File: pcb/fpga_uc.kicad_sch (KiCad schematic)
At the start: 1 part

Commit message: kicad said I needed to save
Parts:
- U?: value (none) -> XC7A100T-FTG256
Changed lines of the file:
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@@
       (effects (font (size 1.27 1.27)) (justify right))
     )
-    (property "Value" "" (id 1) (at 67.31 81.9149 0)
+    (property "Value" "XC7A100T-FTG256" (id 1) (at 67.31 81.9149 0)
       (effects (font (size 1.27 1.27)) (justify right))
     )

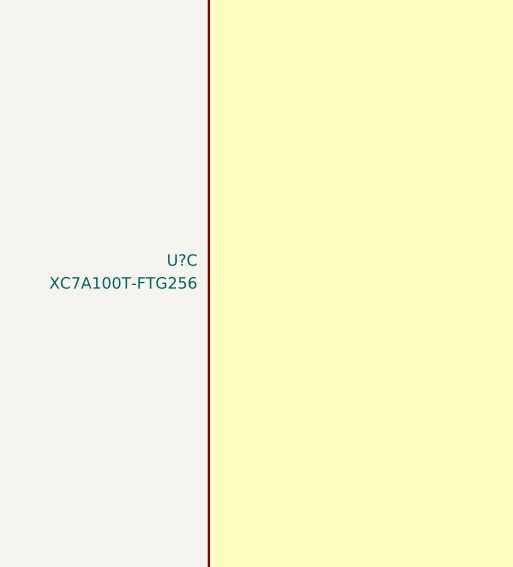
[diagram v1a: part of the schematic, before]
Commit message: add flash memory component for fpga
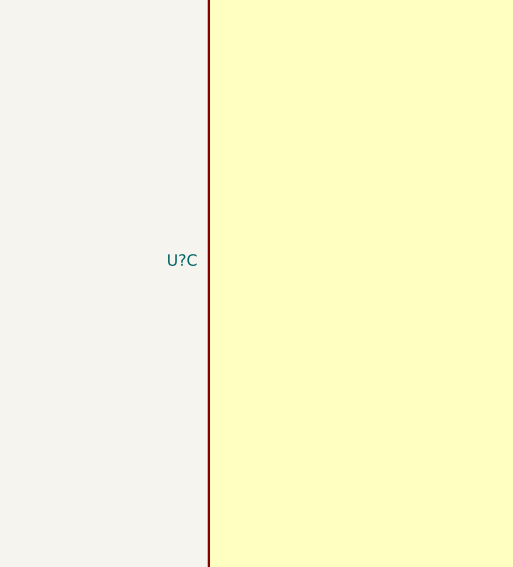
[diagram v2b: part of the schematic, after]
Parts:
- U?: value XC7A100T-FTG256 -> (none)
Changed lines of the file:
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@@
       (effects (font (size 1.27 1.27)) (justify right))
     )
-    (property "Value" "XC7A100T-FTG256" (id 1) (at 67.31 81.9149 0)
+    (property "Value" "" (id 1) (at 67.31 81.9149 0)
       (effects (font (size 1.27 1.27)) (justify right))
     )
